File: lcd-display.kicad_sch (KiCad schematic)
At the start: 7 parts, among them J1 LCD 2004 Female Header, U10 SST39SF040-70-4C-PHE, U9 SST39SF040-70-4C-PHE

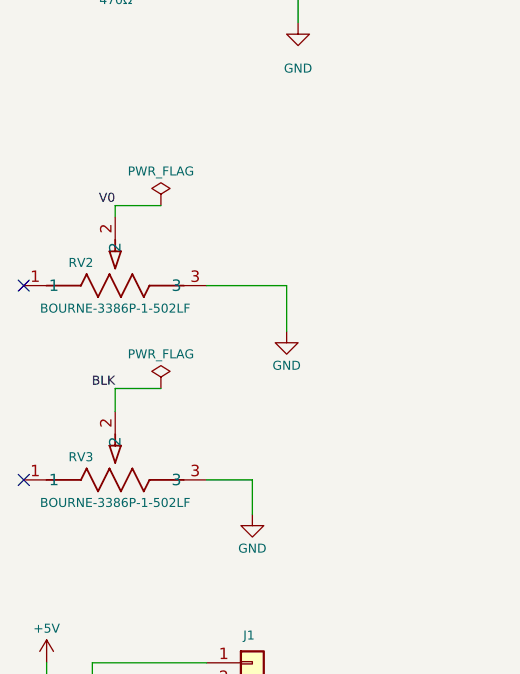
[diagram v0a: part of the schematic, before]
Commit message: Updated symbols/footprint for USB and 5K Trimmer Pots.
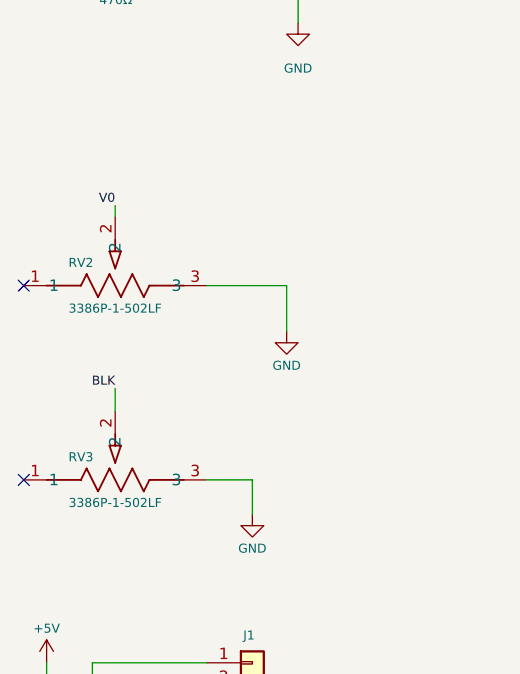
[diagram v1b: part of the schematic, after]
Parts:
- RV2, RV3: value BOURNE-3386P-1-502LF -> 3386P-1-502LF; symbol homebrew_cpu:BOURNE-3386P-1-502LF -> homebrew_cpu:3386P-1-502LF
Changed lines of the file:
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@@
-    (stroke (width 0) (type default))
-  )
-  (wire (pts (xy 39.37 121.92) (xy 44.45 121.92))
     (stroke (width 0) (type default))
   )
@@
   )
   (wire (pts (xy 198.12 31.75) (xy 198.12 55.88))
-    (stroke (width 0) (type default))
-  )
-  (wire (pts (xy 44.45 101.6) (xy 39.37 101.6))
     (stroke (width 0) (type default))
   )
@@
     (effects (font (size 1.27 1.27)) (justify right))
   )
-  (symbol (lib_id "homebrew_cpu:BOURNE-3386P-1-502LF") (at 29.21 110.49 0) (unit 1)
+  (symbol (lib_id "homebrew_cpu:3386P-1-502LF") (at 29.21 110.49 0) (unit 1)
     (in_bom yes) (on_board yes) (dnp no)
     (property "Reference" "RV2" (at 35.56 107.95 0)
       (effects (font (size 1 1)))
     )
-    (property "Value" "BOURNE-3386P-1-502LF" (at 39.37 113.03 0)
+    (property "Value" "3386P-1-502LF" (at 39.37 113.03 0)
       (effects (font (size 1 1)))
     )
     (property "Footprint" "footprints:BOURNE-3386P" (at 29.21 110.49 0)
-      (effects (font (size 1 1) italic) hide)
+      (effects (font (size 1.27 1.27) italic) hide)
     )
     (property "Datasheet" "https://www.bourns.com/docs/Product-Datasheets/3386.pdf" (at 29.21 110.49 0)
-      (effects (font (size 1 1) italic) hide)
+      (effects (font (size 1.27 1.27) italic) hide)
     )
     (property "Manufacturer" "Bourns, Inc." (at 29.21 110.49 0)
-      (effects (font (size 1 1)) hide)
+      (effects (font (size 1.27 1.27)) hide)
     )
     (property "Maunfacturer PN" "3386P-1-502LF" (at 29.21 110.49 0)
-      (effects (font (size 1 1)) hide)
+      (effects (font (size 1.27 1.27)) hide)
     )
     (property "Digikey" "https://www.digikey.com/en/products/detail/bourns-inc/3386P-1-502LF/1088535" (at 29.21 110.49 0)
-      (effects (font (size 1 1)) hide)
+      (effects (font (size 1.27 1.27)) hide)
     )
     (property "Digikey PN" "3386P-502LF-ND" (at 29.21 110.49 0)
-      (effects (font (size 1 1)) hide)
+      (effects (font (size 1.27 1.27)) hide)
     )
     (pin "1")
@@
     )
   )
-  (symbol (lib_id "homebrew_cpu:BOURNE-3386P-1-502LF") (at 29.21 132.08 0) (unit 1)
+  (symbol (lib_id "homebrew_cpu:3386P-1-502LF") (at 29.21 132.08 0) (unit 1)
     (in_bom yes) (on_board yes) (dnp no)
     (property "Reference" "RV3" (at 35.56 129.54 0)
       (effects (font (size 1 1)))
     )
-    (property "Value" "BOURNE-3386P-1-502LF" (at 39.37 134.62 0)
+    (property "Value" "3386P-1-502LF" (at 39.37 134.62 0)
       (effects (font (size 1 1)))
     )
     (property "Footprint" "footprints:BOURNE-3386P" (at 29.21 132.08 0)
-      (effects (font (size 1 1) italic) hide)
+      (effects (font (size 1.27 1.27) italic) hide)
     )
     (property "Datasheet" "https://www.bourns.com/docs/Product-Datasheets/3386.pdf" (at 29.21 132.08 0)
-      (effects (font (size 1 1) italic) hide)
+      (effects (font (size 1.27 1.27) italic) hide)
     )
     (property "Manufacturer" "Bourns, Inc." (at 29.21 132.08 0)
-      (effects (font (size 1 1)) hide)
+      (effects (font (size 1.27 1.27)) hide)
     )
     (property "Maunfacturer PN" "3386P-1-502LF" (at 29.21 132.08 0)
-      (effects (font (size 1 1)) hide)
+      (effects (font (size 1.27 1.27)) hide)
     )
     (property "Digikey" "https://www.digikey.com/en/products/detail/bourns-inc/3386P-1-502LF/1088535" (at 29.21 132.08 0)
-      (effects (font (size 1 1)) hide)
+      (effects (font (size 1.27 1.27)) hide)
     )
     (property "Digikey PN" "3386P-502LF-ND" (at 29.21 132.08 0)
-      (effects (font (size 1 1)) hide)
+      (effects (font (size 1.27 1.27)) hide)
     )
     (pin "1")
@@
         )
       )
-    )
-  )
-  (symbol (lib_id "power:PWR_FLAG") (at 44.45 101.6 0) (unit 1)
-    (in_bom yes) (on_board yes) (dnp no)
-    (property "Reference" "#FLG05" (at 44.45 99.695 0)
-      (effects (font (size 1 1)) hide)
-    )
-    (property "Value" "PWR_FLAG" (at 44.45 97.79 0)
-      (effects (font (size 1 1)))
-    )
-    (property "Footprint" "" (at 44.45 101.6 0)
-      (effects (font (size 1 1)) hide)
-    )
-    (property "Datasheet" "~" (at 44.45 101.6 0)
-      (effects (font (size 1 1)) hide)
-    )
-    (pin "1")
-    (instances
-      (project "cpu"
-        (path "/7aab8e99-eed8-4c64-b2cd-ed9d372ca98a/782dca9d-92a1-4994-813f-8702f7c063a6"
-          (reference "#FLG05") (unit 1)
-        )
-      )
-    )
-  )
-  (symbol (lib_id "power:PWR_FLAG") (at 44.45 121.92 0) (unit 1)
-    (in_bom yes) (on_board yes) (dnp no)
-    (property "Reference" "#FLG04" (at 44.45 120.015 0)
-      (effects (font (size 1 1)) hide)
-    )
-    (property "Value" "PWR_FLAG" (at 44.45 118.11 0)
-      (effects (font (size 1 1)))
-    )
-    (property "Footprint" "" (at 44.45 121.92 0)
-      (effects (font (size 1 1)) hide)
-    )
-    (property "Datasheet" "~" (at 44.45 121.92 0)
-      (effects (font (size 1 1)) hide)
-    )
-    (pin "1")
-    (instances
-      (project "cpu"
-        (path "/7aab8e99-eed8-4c64-b2cd-ed9d372ca98a/782dca9d-92a1-4994-813f-8702f7c063a6"
-          (reference "#FLG04") (unit 1)
-        )
-      )

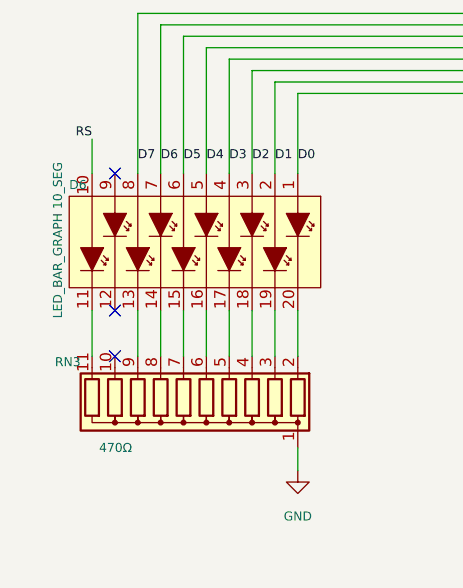
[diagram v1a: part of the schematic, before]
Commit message: Final changes around adding BOM to README.md
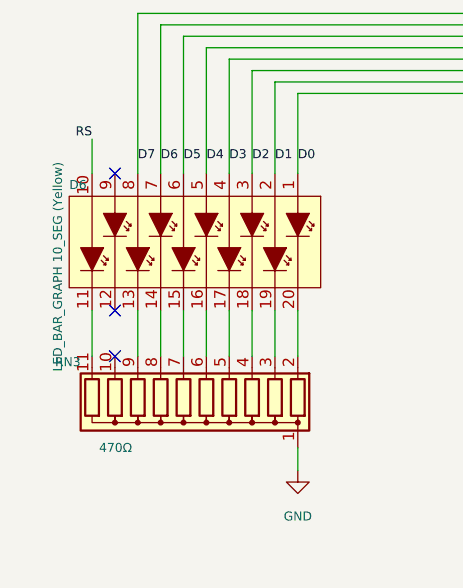
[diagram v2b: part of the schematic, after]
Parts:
- D6: value LED_BAR_GRAPH 10_SEG -> LED_BAR_GRAPH 10_SEG (Yellow)
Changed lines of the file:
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@@
       (effects (font (size 1 1)) (justify left))
     )
-    (property "Value" "LED_BAR_GRAPH  10_SEG" (at 33.02 46.99 0)
+    (property "Value" "LED_BAR_GRAPH  10_SEG (Yellow)" (at 33.02 46.99 0)
       (effects (font (size 1 1)) (justify left))
     )

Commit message: V1.1-last Kicad v7 version
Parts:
- D6: footprint footprints:LED_Bar_Graph_10_SEG -> Homebrew-CPU-PCB:LED_Bar_Graph_10_SEG; symbol homebrew_cpu:LED_BAR_GRAPH_10_SEG -> Homebrew-CPU-PCB:LED_BAR_GRAPH_10_SEG
- J1: footprint footprints:LCD_2004_PinSocket_1x16_P2.54mm_Vertical -> Homebrew-CPU-PCB:LCD_2004_PinSocket_1x16_P2.54mm_Vertical; symbol homebrew_cpu:LCD_2004_PinSocket_1x16_P2.54mm_Vertical -> Homebrew-CPU-PCB:LCD_2004_PinSocket_1x16_P2.54mm_Vertical
- RN3: footprint footprints:R_Array_SIP11 -> Homebrew-CPU-PCB:R_Array_SIP11; symbol homebrew_cpu:R_Network10 -> Homebrew-CPU-PCB:R_Network10
- RV2, RV3: footprint footprints:BOURNE-3386P -> Homebrew-CPU-PCB:BOURNE-3386P; symbol homebrew_cpu:3386P-1-502LF -> Homebrew-CPU-PCB:3386P-1-502LF
- U10, U9: footprint footprints:PDIP32_PH_SST_MCH -> Homebrew-CPU-PCB:PDIP32_PH_SST_MCH; symbol homebrew_cpu:SST39SF040-70-4C-PHE -> Homebrew-CPU-PCB:SST39SF040-70-4C-PHE
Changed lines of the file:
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@@
     (effects (font (size 1.27 1.27)) (justify right))
   )
-  (symbol (lib_id "homebrew_cpu:3386P-1-502LF") (at 29.21 110.49 0) (unit 1)
+  (symbol (lib_name "3386P-1-502LF_1") (lib_id "Homebrew-CPU-PCB:3386P-1-502LF") (at 29.21 110.49 0) (unit 1)
     (in_bom yes) (on_board yes) (dnp no)
     (property "Reference" "RV2" (at 35.56 107.95 0)
@@
       (effects (font (size 1 1)))
     )
-    (property "Footprint" "footprints:BOURNE-3386P" (at 29.21 110.49 0)
+    (property "Footprint" "Homebrew-CPU-PCB:BOURNE-3386P" (at 29.21 110.49 0)
       (effects (font (size 1.27 1.27) italic) hide)
     )
@@
     )
   )
-  (symbol (lib_id "homebrew_cpu:3386P-1-502LF") (at 29.21 132.08 0) (unit 1)
+  (symbol (lib_id "Homebrew-CPU-PCB:3386P-1-502LF") (at 29.21 132.08 0) (unit 1)
     (in_bom yes) (on_board yes) (dnp no)
     (property "Reference" "RV3" (at 35.56 129.54 0)
@@
       (effects (font (size 1 1)))
     )
-    (property "Footprint" "footprints:BOURNE-3386P" (at 29.21 132.08 0)
+    (property "Footprint" "Homebrew-CPU-PCB:BOURNE-3386P" (at 29.21 132.08 0)
       (effects (font (size 1.27 1.27) italic) hide)
     )
@@
     )
   )
-  (symbol (lib_id "homebrew_cpu:R_Network10") (at 46.99 73.66 180) (unit 1)
+  (symbol (lib_id "Homebrew-CPU-PCB:R_Network10") (at 46.99 73.66 180) (unit 1)
     (in_bom yes) (on_board yes) (dnp no)
     (property "Reference" "RN3" (at 35.56 69.215 0)
@@
       (effects (font (size 1 1)) (justify left))
     )
-    (property "Footprint" "footprints:R_Array_SIP11" (at 32.385 73.66 90)
+    (property "Footprint" "Homebrew-CPU-PCB:R_Array_SIP11" (at 32.385 73.66 90)
       (effects (font (size 1 1)) hide)
     )
@@
     )
   )
-  (symbol (lib_id "homebrew_cpu:LCD_2004_PinSocket_1x16_P2.54mm_Vertical") (at 54.61 170.18 0) (unit 1)
+  (symbol (lib_id "Homebrew-CPU-PCB:LCD_2004_PinSocket_1x16_P2.54mm_Vertical") (at 54.61 170.18 0) (unit 1)
     (in_bom yes) (on_board yes) (dnp no)
     (property "Reference" "J1" (at 53.594 149.352 0)
@@
       (effects (font (size 1 1)) (justify right))
     )
-    (property "Footprint" "footprints:LCD_2004_PinSocket_1x16_P2.54mm_Vertical" (at 54.61 170.18 0)
+    (property "Footprint" "Homebrew-CPU-PCB:LCD_2004_PinSocket_1x16_P2.54mm_Vertical" (at 54.61 170.18 0)
       (effects (font (size 1 1)) hide)
     )
@@
     )
   )
-  (symbol (lib_id "homebrew_cpu:LED_BAR_GRAPH_10_SEG") (at 59.69 55.88 270) (unit 1)
+  (symbol (lib_id "Homebrew-CPU-PCB:LED_BAR_GRAPH_10_SEG") (at 59.69 55.88 270) (unit 1)
     (in_bom yes) (on_board yes) (dnp no)
     (property "Reference" "D6" (at 34.29 49.53 90)
@@
       (effects (font (size 1 1)) (justify left))
     )
-    (property "Footprint" "footprints:LED_Bar_Graph_10_SEG" (at 64.77 60.96 0)
+    (property "Footprint" "Homebrew-CPU-PCB:LED_Bar_Graph_10_SEG" (at 64.77 60.96 0)
       (effects (font (size 1 1)) (justify left) hide)
     )
@@
     )
   )
-  (symbol (lib_id "homebrew_cpu:SST39SF040-70-4C-PHE") (at 93.98 72.39 0) (unit 1)
+  (symbol (lib_id "Homebrew-CPU-PCB:SST39SF040-70-4C-PHE") (at 93.98 72.39 0) (unit 1)
     (in_bom yes) (on_board yes) (dnp no) (fields_autoplaced)
     (property "Reference" "U9" (at 114.3 62.865 0)
@@
       (effects (font (size 1 1)))
     )
-    (property "Footprint" "footprints:PDIP32_PH_SST_MCH" (at 85.725 69.85 0)
+    (property "Footprint" "Homebrew-CPU-PCB:PDIP32_PH_SST_MCH" (at 85.725 69.85 0)
       (effects (font (size 1 1) italic) hide)
     )
@@
     )
   )
-  (symbol (lib_id "homebrew_cpu:SST39SF040-70-4C-PHE") (at 217.17 43.18 0) (unit 1)
+  (symbol (lib_name "SST39SF040-70-4C-PHE_1") (lib_id "Homebrew-CPU-PCB:SST39SF040-70-4C-PHE") (at 217.17 43.18 0) (unit 1)
     (in_bom yes) (on_board yes) (dnp no) (fields_autoplaced)
     (property "Reference" "U10" (at 237.49 33.655 0)
@@
       (effects (font (size 1 1)))
     )
-    (property "Footprint" "footprints:PDIP32_PH_SST_MCH" (at 208.915 40.64 0)
+    (property "Footprint" "Homebrew-CPU-PCB:PDIP32_PH_SST_MCH" (at 208.915 40.64 0)
       (effects (font (size 1 1) italic) hide)
     )
